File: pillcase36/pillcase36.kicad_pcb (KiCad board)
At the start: 2 copper layers, 114 x 140.5 mm, 125 parts, among them J1 AudioJack4_Ground, SW1 SW_Push, SW10 SW_Push, SW11 SW_Push, SW12 SW_Push, SW13 SW_Push, SW14 SW_Push, SW15 SW_Push, SW16 SW_Push, SW17 SW_Push, SW18 SW_Push, SW19 SW_Push, SW2 SW_Push, SW20 SW_Push, SW21 SW_Push, SW22 SW_Push, SW23 SW_Push, SW24 SW_Push, SW25 SW_Push, SW26 SW_Push, SW27 SW_Push, SW28 SW_Push, SW29 SW_Push, SW3 SW_Push, SW30 SW_Push, SW31 SW_Push, SW32 SW_Push, SW33 SW_Push, SW34 SW_Push, SW35 SW_Push, SW36 SW_Push, SW37 SW_Push, SW4 SW_Push, SW5 SW_Push, SW6 SW_Push, SW7 SW_Push, SW8 SW_Push, SW9 SW_Push, U1 BlackPill, U2 24LC00

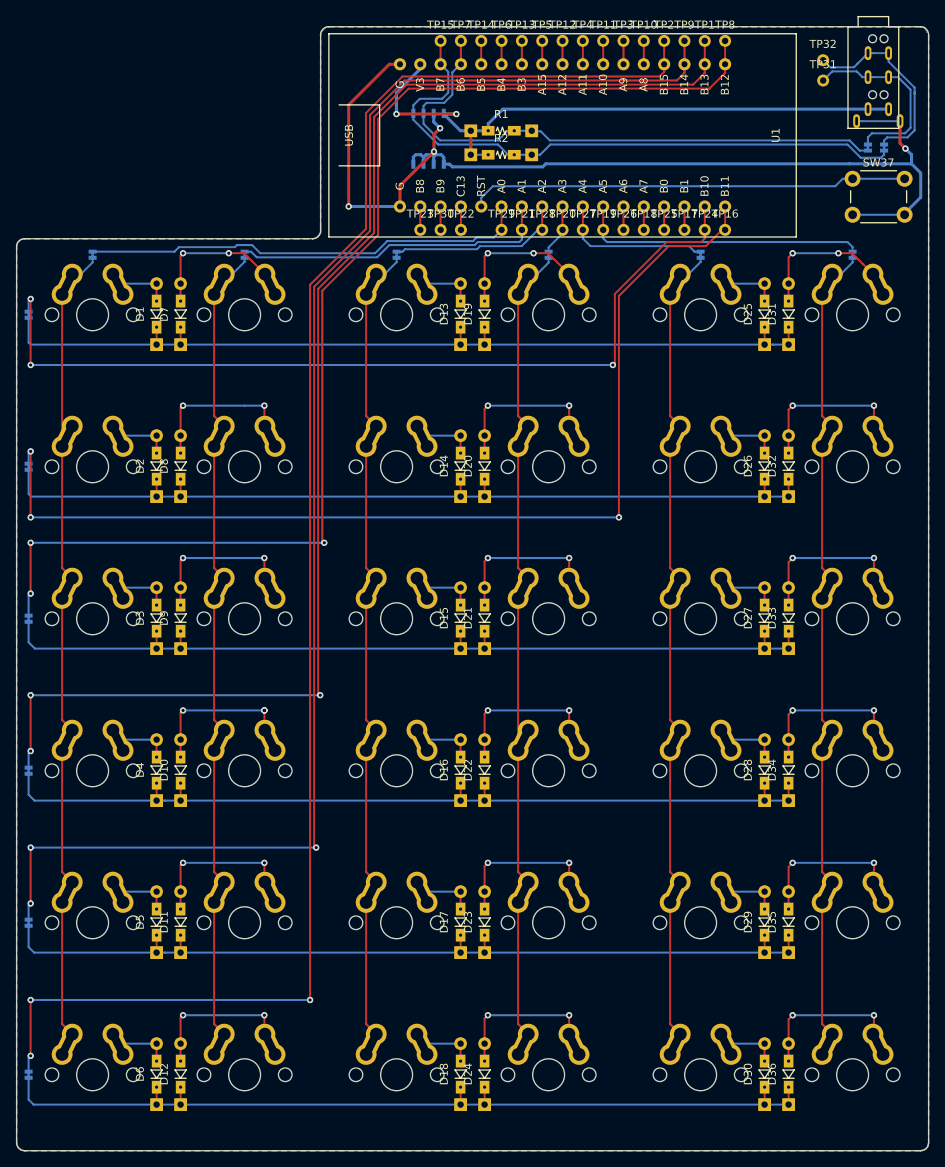
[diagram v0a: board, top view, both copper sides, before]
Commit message: Tune routing further, fix silkscreen label positions
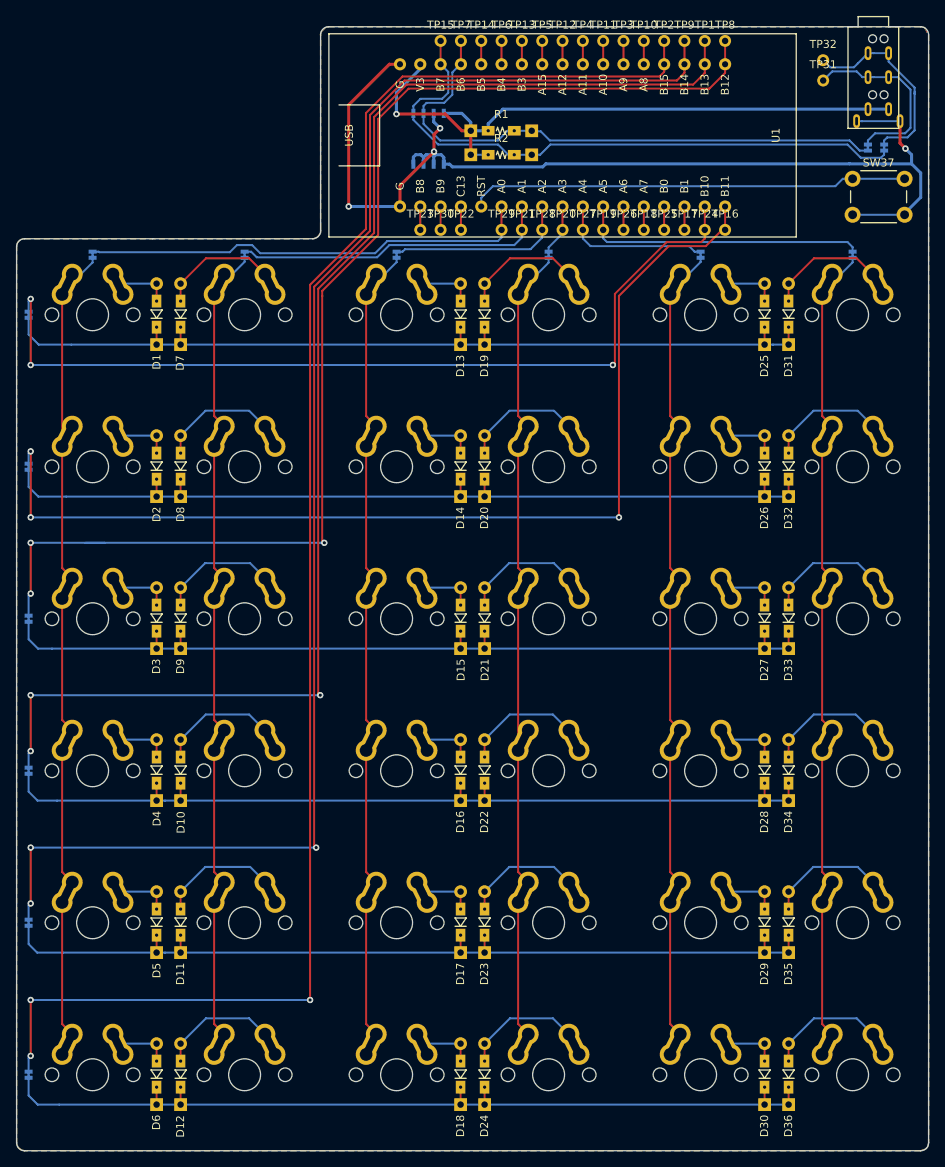
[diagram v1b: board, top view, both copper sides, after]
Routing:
- net Net-(D32-Pad2): track 18.9 -> 14.8 mm, vias 2 -> 0
- net Net-(D33-Pad2): track 18.8 -> 14.8 mm, vias 2 -> 0
- net Net-(D8-Pad2): track 18.8 -> 14.8 mm, vias 2 -> 0
- net Net-(D20-Pad2): track 18.8 -> 14.8 mm, vias 2 -> 0
- net Net-(D21-Pad2): track 18.7 -> 14.8 mm, vias 2 -> 0
- net Net-(D22-Pad2): track 18.6 -> 14.8 mm, vias 2 -> 0
- net Net-(D23-Pad2): track 18.5 -> 14.8 mm, vias 2 -> 0
- net Net-(D11-Pad2): track 18.5 -> 14.8 mm, vias 2 -> 0
- net Net-(D24-Pad2): track 18.4 -> 14.9 mm, vias 2 -> 0
- net Net-(D12-Pad2): track 18.4 -> 14.9 mm, vias 2 -> 0
- net Net-(D19-Pad2): track 17.4 -> 14.8 mm, vias 2 -> 0
- net Net-(D34-Pad2): track 18.7 -> 16.2 mm, vias 2 -> 0
- net ROW2: track 151.8 -> 154.2 mm
- net Net-(D9-Pad2): track 18.7 -> 16.3 mm, vias 2 -> 0
- net Net-(D35-Pad2): track 18.6 -> 16.3 mm, vias 2 -> 0
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
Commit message: Finish reroute, ready pull request
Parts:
- moved R1 2.65 mm to (104.6, 51.8)
- moved R2 2.63 mm to (104.6, 55.1)
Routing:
- net VCC: track 81.6 -> 83.8 mm
- net GND: track 134.7 -> 135.6 mm

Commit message: main_v1.0 release
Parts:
- removed the G*** at (142.3, 53.6)
- removed JP1, JP10, JP11, JP12, JP2, JP3, JP4, JP5, JP6, JP7, JP8, JP9: SolderJumper_2_Bridged, pillcase36:JP
- added 0.1u: C, Capacitors_SMD:C_0603, B.Cu at (101.6, 50.6)
- added ?: , pillcase36:Hole_5mm, F.Cu at (103.5, 122.5)
- added G***: pillcase36_logo, pillcase36:pillcase36_logo, B.Cu at (125.2, 52.9)
- added G***: pillcase36_logo, pillcase36:pillcase36_logo, F.Cu at (125.2, 52.8)
- SCL1 : renamed from JP14
- renumbered TP31 to R1, TP32 to R2, SW37 to RESET, JP13 to SDA1
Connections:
- D1 pad 1: Net-(D1-Pad1) -> ROW0
- D10 pad 1: Net-(D10-Pad1) -> ROW3
- D11 pad 1: Net-(D11-Pad1) -> ROW4
- D12 pad 1: Net-(D12-Pad1) -> ROW5
- D13 pad 1: Net-(D1-Pad1) -> ROW0
- D14 pad 1: Net-(D14-Pad1) -> ROW1
- D15 pad 1: Net-(D15-Pad1) -> ROW2
- D16 pad 1: Net-(D10-Pad1) -> ROW3
- D17 pad 1: Net-(D11-Pad1) -> ROW4
- D18 pad 1: Net-(D12-Pad1) -> ROW5
- D19 pad 1: Net-(D1-Pad1) -> ROW0
- D2 pad 1: Net-(D14-Pad1) -> ROW1
- D20 pad 1: Net-(D14-Pad1) -> ROW1
- D21 pad 1: Net-(D15-Pad1) -> ROW2
- D22 pad 1: Net-(D10-Pad1) -> ROW3
- D23 pad 1: Net-(D11-Pad1) -> ROW4
- D24 pad 1: Net-(D12-Pad1) -> ROW5
- D25 pad 1: Net-(D1-Pad1) -> ROW0
- D26 pad 1: Net-(D14-Pad1) -> ROW1
- D27 pad 1: Net-(D15-Pad1) -> ROW2
- D28 pad 1: Net-(D10-Pad1) -> ROW3
- D29 pad 1: Net-(D11-Pad1) -> ROW4
- D3 pad 1: Net-(D15-Pad1) -> ROW2
- D30 pad 1: Net-(D12-Pad1) -> ROW5
- D31 pad 1: Net-(D1-Pad1) -> ROW0
- D32 pad 1: Net-(D14-Pad1) -> ROW1
- D33 pad 1: Net-(D15-Pad1) -> ROW2
- D34 pad 1: Net-(D10-Pad1) -> ROW3
- D35 pad 1: Net-(D11-Pad1) -> ROW4
- D36 pad 1: Net-(D12-Pad1) -> ROW5
- D4 pad 1: Net-(D10-Pad1) -> ROW3
- D5 pad 1: Net-(D11-Pad1) -> ROW4
- D6 pad 1: Net-(D12-Pad1) -> ROW5
- D7 pad 1: Net-(D1-Pad1) -> ROW0
- D8 pad 1: Net-(D14-Pad1) -> ROW1
- D9 pad 1: Net-(D15-Pad1) -> ROW2
- SW1 pad 1: Net-(JP7-Pad2) -> COL0
- SW10 pad 1: Net-(JP8-Pad2) -> COL1
- SW11 pad 1: Net-(JP8-Pad2) -> COL1
- SW12 pad 1: Net-(JP8-Pad2) -> COL1
- SW13 pad 1: Net-(JP9-Pad2) -> COL2
- SW14 pad 1: Net-(JP9-Pad2) -> COL2
- SW15 pad 1: Net-(JP9-Pad2) -> COL2
- SW16 pad 1: Net-(JP9-Pad2) -> COL2
- SW17 pad 1: Net-(JP9-Pad2) -> COL2
- SW18 pad 1: Net-(JP9-Pad2) -> COL2
- SW19 pad 1: Net-(JP10-Pad2) -> COL3
- SW2 pad 1: Net-(JP7-Pad2) -> COL0
- SW20 pad 1: Net-(JP10-Pad2) -> COL3
- SW21 pad 1: Net-(JP10-Pad2) -> COL3
- SW22 pad 1: Net-(JP10-Pad2) -> COL3
- SW23 pad 1: Net-(JP10-Pad2) -> COL3
- SW24 pad 1: Net-(JP10-Pad2) -> COL3
- SW25 pad 1: Net-(JP11-Pad2) -> COL4
- SW26 pad 1: Net-(JP11-Pad2) -> COL4
- SW27 pad 1: Net-(JP11-Pad2) -> COL4
- SW28 pad 1: Net-(JP11-Pad2) -> COL4
- SW29 pad 1: Net-(JP11-Pad2) -> COL4
- SW3 pad 1: Net-(JP7-Pad2) -> COL0
- SW30 pad 1: Net-(JP11-Pad2) -> COL4
- SW31 pad 1: Net-(JP12-Pad2) -> COL5
- SW32 pad 1: Net-(JP12-Pad2) -> COL5
- SW33 pad 1: Net-(JP12-Pad2) -> COL5
- SW34 pad 1: Net-(JP12-Pad2) -> COL5
- SW35 pad 1: Net-(JP12-Pad2) -> COL5
- SW36 pad 1: Net-(JP12-Pad2) -> COL5
- SW4 pad 1: Net-(JP7-Pad2) -> COL0
- SW5 pad 1: Net-(JP7-Pad2) -> COL0
- SW6 pad 1: Net-(JP7-Pad2) -> COL0
- SW7 pad 1: Net-(JP8-Pad2) -> COL1
- SW8 pad 1: Net-(JP8-Pad2) -> COL1
- SW9 pad 1: Net-(JP8-Pad2) -> COL1
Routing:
- net Net-(D11-Pad1): track 110.8 -> 0.00 mm
- net Net-(D10-Pad1): track 110.8 -> 0.00 mm
- net Net-(D12-Pad1): track 110.8 -> 0.00 mm
- net Net-(D15-Pad1): track 110.7 -> 0.00 mm
- net Net-(D14-Pad1): track 110.7 -> 0.00 mm
- net Net-(D1-Pad1): track 110.7 -> 0.00 mm
- net COL3: track 6.56 -> 97.8 mm
- net Net-(JP7-Pad2): track 90.8 -> 0.00 mm
- net Net-(JP10-Pad2): track 90.7 -> 0.00 mm
- net COL5: track 36.4 -> 126.8 mm
- net COL4: track 19.6 -> 109.9 mm
- net Net-(JP12-Pad2): track 89.8 -> 0.00 mm
- net Net-(JP11-Pad2): track 89.8 -> 0.00 mm
- net COL0: track 56.8 -> 146.5 mm
- net COL2: track 23.0 -> 111.8 mm
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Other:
- board text added: "PILLCASE36 v1.0 @Pekaso 2018 Self-Made Keyboards in Japan Dicord Group"

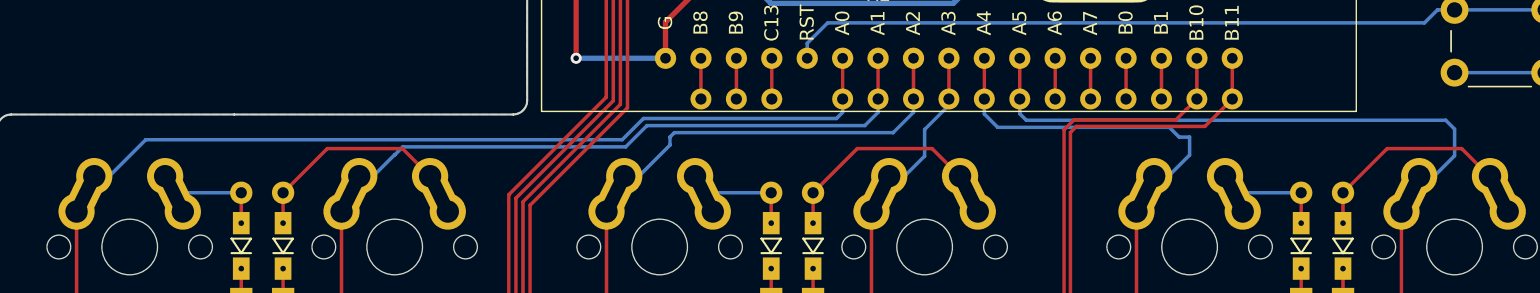
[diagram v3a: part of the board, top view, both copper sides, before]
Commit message: Straighten a few squiggly traces
Where the jumpers used to be
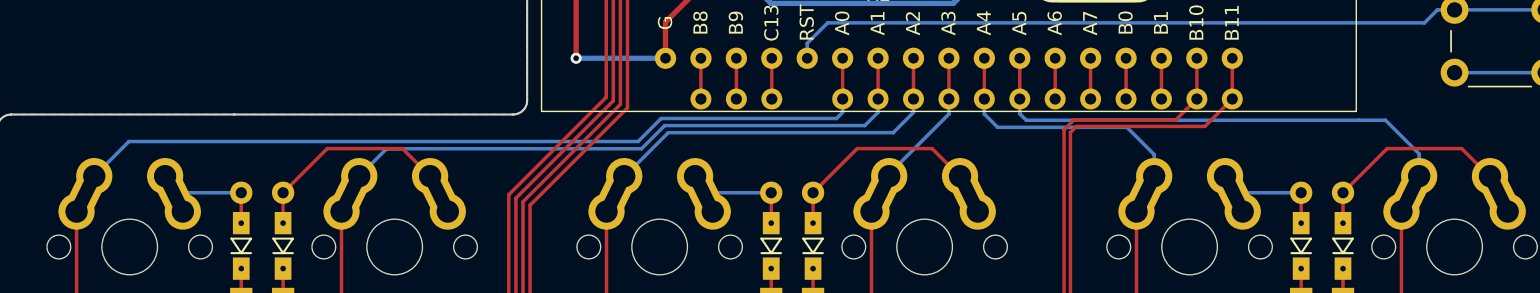
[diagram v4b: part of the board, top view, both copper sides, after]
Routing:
- net COL5: track 126.8 -> 120.8 mm
- net COL4: track 109.9 -> 104.2 mm
- net COL0: track 146.5 -> 145.8 mm
- net COL3: track 97.8 -> 97.2 mm
